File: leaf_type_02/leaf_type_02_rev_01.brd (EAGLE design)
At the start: 35.4 x 21.2 mm, 25 parts, among them J1 TC_2050_IDC_NL_TOP, J3 CONN_4X1_JST_PA, J4 CONN_4X1_JST_PA, J5 CONN_4X1_LEAF_SMT, U2 RS485_XCVR_SN65HVD178X

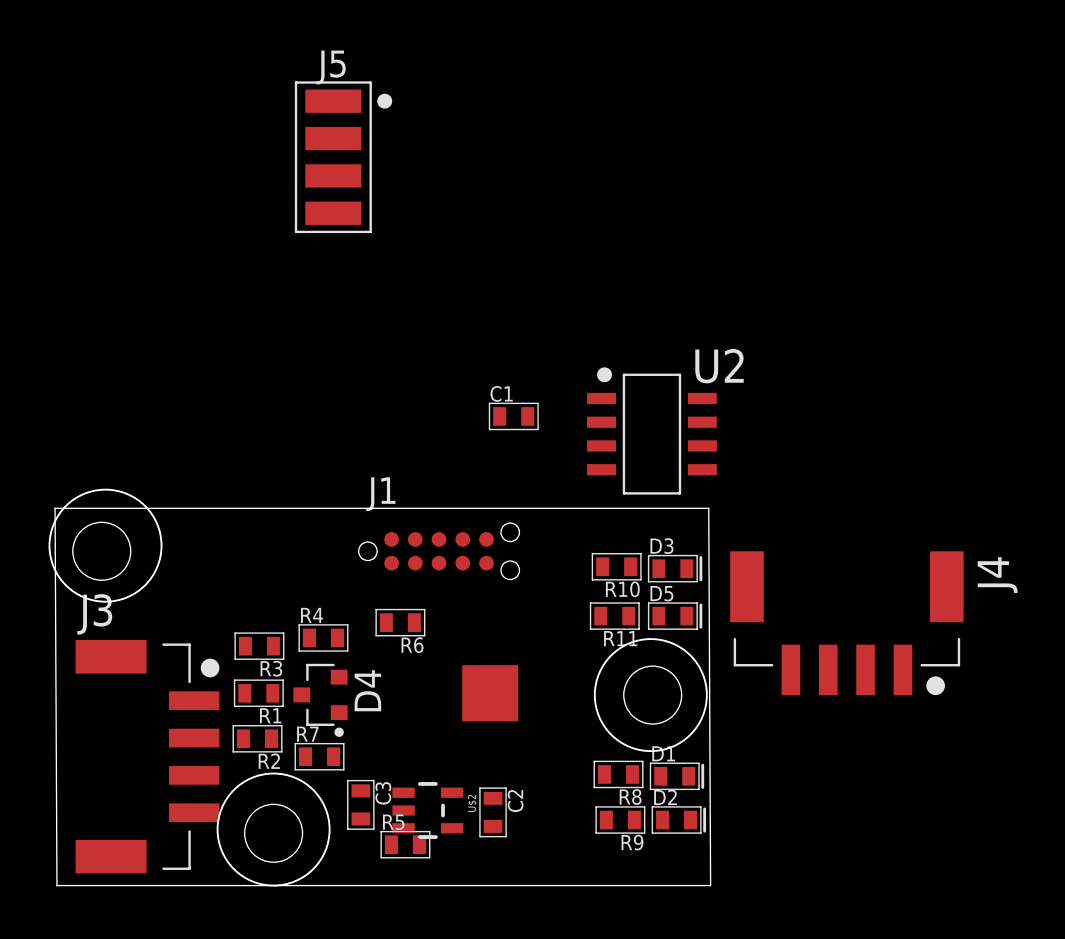
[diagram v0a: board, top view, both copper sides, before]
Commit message: updated library & type 02
fixed some of the sizes of device names, updates rs485 tx & rx drivers
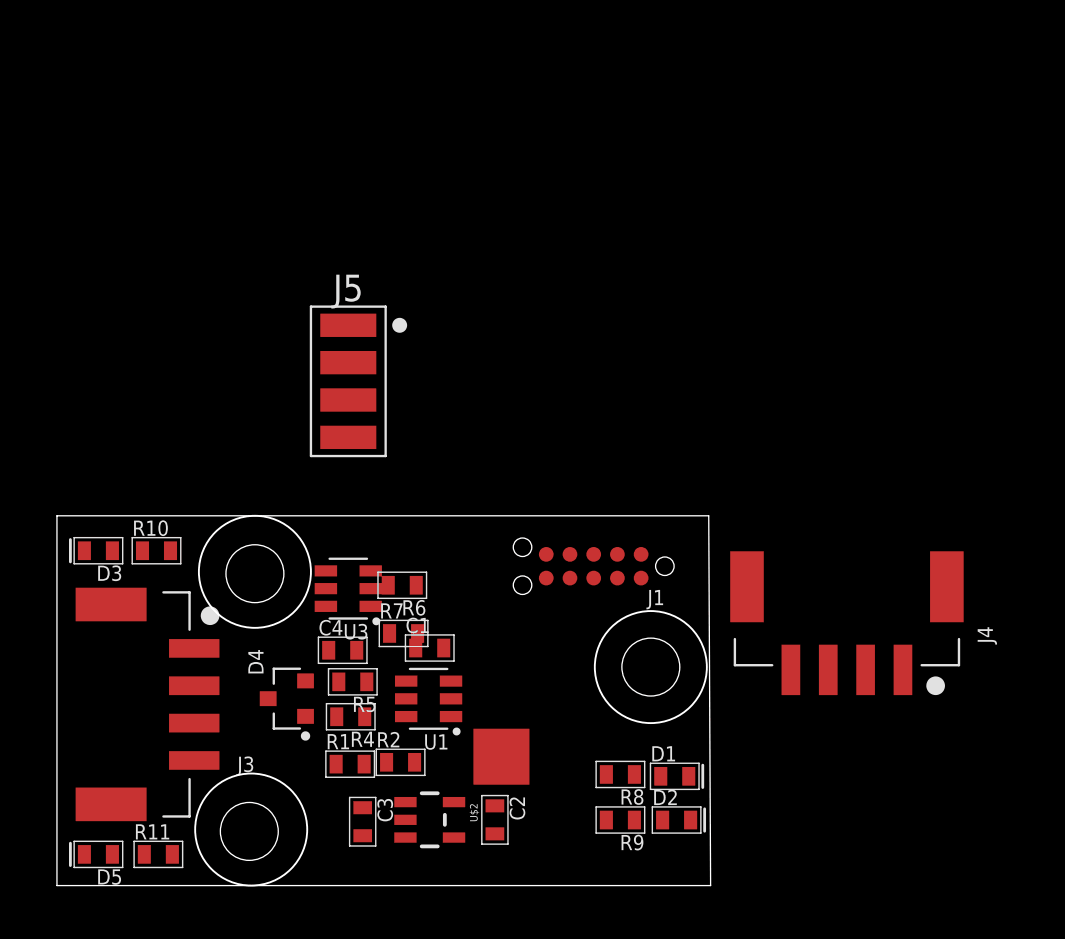
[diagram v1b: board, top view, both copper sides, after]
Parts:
- removed R3: (no value), stepOSP:0603
- removed U2: RS485_XCVR_SN65HVD178X, leaf:SOIC_08_TI
- added C4: 0.1u, stepOSP:0603
- added U1: RS485_RCVR_ISL32612E, leaf:SOT23-6_INTERSIL
- added U3: RS485_TCVR_ISL32614E, leaf:SOT23-6_INTERSIL
- R1: value 120 -> 3.3k
- R2: value (none) -> NP
- R6: value 3.3k -> NP
- moved D5 33.3 mm to (2.22, 1.67), turned to 180 degrees
- moved D3 30.8 mm to (2.22, 17.9), turned to 180 degrees
- moved R11 27.6 mm to (5.43, 1.67), turned to 0 degrees
- moved R10 24.7 mm to (5.33, 17.9), turned to 0 degrees
- moved J1 15.9 mm to (32.5, 17.1), turned to 180 degrees
- moved C1 13.2 mm to (20.0, 12.7)
- moved J5 12.0 mm to (15.6, 27.0)
- moved R5 9.16 mm to (15.8, 10.9), turned to 180 degrees
- moved R7 7.99 mm to (18.6, 13.5)
- moved R2 7.76 mm to (18.4, 6.60), turned to 0 degrees
- moved R1 6.19 mm to (15.7, 6.50), turned to 0 degrees
- moved R4 4.47 mm to (15.7, 9.04), turned to 180 degrees
- moved J3 2.80 mm to (-1.80, 9.70)
- moved R6 2.00 mm to (18.5, 16.1)
- moved D4 1.81 mm to (12.3, 10.0)
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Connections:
- removed net N$10: U2.4
- removed net N$6: D4.2, R1.P$1, R3.P$2, R4.P$2
- removed net N$9: R6.P$1, U2.1
- new net RX: R2.P$1, U1.3
- new net RXE: R1.P$2, R6.P$1, U1.5
- new net TX: U3.1
- new net TXE: R7.P$2, U3.3
- net +3V3: now also C4.P$1, U1.1, U3.2; no longer U2.8
- net GND1: now also C4.P$2, J5.1, R1.P$1, U1.2, U3.5; no longer R3.P$1, U2.5
- net N$1: now also U1.6, U3.6; no longer U2.6
- net N$2: now also U1.4, U3.4; no longer U2.7
- net N$7: now also D4.2, J5.3; no longer D4.1, R1.P$2, R2.P$1
- net N$8: now also D4.1, J5.2, R4.P$2; no longer R7.P$2, U2.2, U2.3
- net V+: now also J5.4
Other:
- board size 35.4 x 21.2 mm -> 35 x 19.8 mm

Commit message: added to library GH connector and updated 0x02 board layout
gh connector only can handle 1A which isn't great but very small
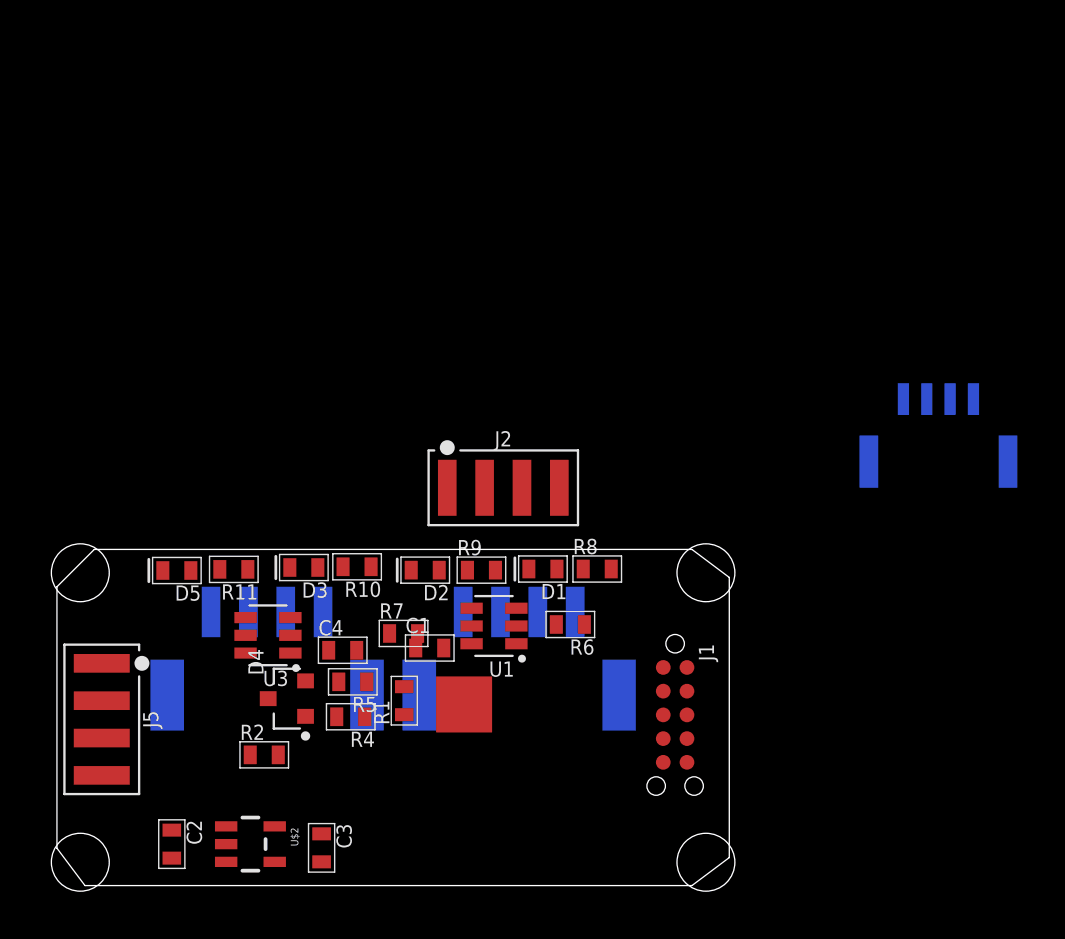
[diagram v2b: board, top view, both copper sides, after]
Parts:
- added J2: CONN_4X1_LEAF_SMT, leaf:CONN_4X1_LEAF_SMT
- added J6: CONN_4X1_JST_GH, leaf:CONN_4X1_JST_GH
- moved J4 34.6 mm to (11.2, 5.50), flipped to the bottom, turned to 180 degrees
- moved J3 26.9 mm to (24.8, 5.50), flipped to the bottom, turned to 180 degrees
- moved J5 22.4 mm to (2.40, 8.90)
- moved D2 19.0 mm to (19.7, 16.9), turned to 180 degrees
- moved C2 17.3 mm to (6.15, 2.22)
- moved R11 15.8 mm to (9.47, 16.9), turned to 180 degrees
- moved D5 15.8 mm to (6.42, 16.9)
- moved R9 15.3 mm to (22.7, 16.9), turned to 0 degrees
- moved D1 13.2 mm to (26.0, 16.9), turned to 180 degrees
- moved R8 11.1 mm to (28.9, 16.9), turned to 0 degrees
- moved D3 11.0 mm to (13.2, 17.0)
- moved R10 10.8 mm to (16.1, 17.1), turned to 180 degrees
- moved U$2 9.69 mm to (10.4, 2.22)
- moved R6 9.24 mm to (27.5, 14.0)
- moved R2 7.31 mm to (11.1, 7.00)
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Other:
- board size 35 x 19.8 mm -> 36 x 18 mm

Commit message: WORK IN PROGRESS
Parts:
- removed C1: 0.1u, stepOSP:0603
- removed J1: TC_2050_IDC_NL_TOP, leaf:TC_2050_IDC_NL_TOP
- removed J4: CONN_4X1_JST_PA, leaf:CONN_4X1_JST_PA
- removed J5: CONN_4X1_LEAF_SMT, leaf:CONN_4X1_LEAF_SMT
- removed R2, R6: NP, stepOSP:0603
- removed U3: RS485_TCVR_ISL32614E, leaf:SOT23-6_INTERSIL
- J2: value CONN_4X1_LEAF_SMT -> TC_2030_IDC_NL_TOP; device leaf:CONN_4X1_LEAF_SMT -> leaf:TC_2030_IDC_NL_TOP
- J3: value CONN_4X1_JST_PA -> CONN_4X1_JST_GH; device leaf:CONN_4X1_JST_PA -> leaf:CONN_4X1_JST_GH
- U1: value RS485_RCVR_ISL32612E -> RS485_XCVR_SN65HVD178X; device leaf:SOT23-6_INTERSIL -> leaf:SOIC_08_TI
- moved J6 32.0 mm to (19.2, 5.90)
- moved U1 18.8 mm to (5.80, 7.40), turned to 0 degrees
- moved J2 16.4 mm to (27.8, 5.40), turned to 90 degrees
- moved J3 15.6 mm to (9.20, 5.90)
- moved D5 15.0 mm to (21.1, 13.7), turned to 270 degrees
- moved R5 14.4 mm to (2.04, 6.71)
- moved C3 14.2 mm to (5.43, 13.2), turned to 90 degrees
- moved R1 14.1 mm to (6.80, 2.10), turned to 0 degrees
- moved R4 13.9 mm to (1.87, 10.6)
- moved R11 13.3 mm to (21.2, 10.6), turned to 90 degrees
- moved C2 11.7 mm to (8.45, 13.7)
- moved U$2 11.5 mm to (12.7, 13.5)
- moved D4 10.8 mm to (1.89, 6.99), flipped to the bottom, turned to 270 degrees
- moved R7 10.8 mm to (11.5, 5.36), turned to 90 degrees
- moved D3 10.2 mm to (22.9, 13.7), turned to 270 degrees
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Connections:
- removed net N$11: D5.P$1, R11.P$1
- removed net N$8: D4.1, J5.2, R4.P$2
- removed net RX: R2.P$1, U1.3
- removed net RXE: R1.P$2, R6.P$1, U1.5
- removed net TX: U3.1
- removed net TXE: R7.P$2, U3.3
- new net N$10: R7.P$2, U1.2, U1.3
- new net N$12: R1.P$1, U1.1
- new net N$13: U1.4
- new net N$6: R4.P$1, U1.7
- new net N$9: R5.P$1, U1.6
- net +3V3: now also D1.P$1, D2.P$1, D3.P$1, D5.P$1, R1.P$2, U1.8; no longer C1.P$1, R2.P$2, R6.P$2, U1.1, U3.2
- net GND1: now also J3.1, J6.1, U1.5; no longer C1.P$2, J5.1, R1.P$1, U1.2, U3.5
- net N$1: now also D4.1, J3.3, J6.3, R4.P$2; no longer R4.P$1, U1.6, U3.6
- net N$2: now also D1.P$2, R8.P$2; no longer R5.P$1, U1.4, U3.4
- net N$3: now also D2.P$2, R9.P$2; no longer D1.P$1, R8.P$1
- net N$4: now also D3.P$2, R10.P$2; no longer D2.P$1, R9.P$1
- net N$5: now also D5.P$2, R11.P$2; no longer D3.P$1, R10.P$1
- net N$7: now also J3.2, J6.2; no longer J5.3
- net V+: now also J3.4; no longer J5.4
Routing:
- net N$1: track 0.00 -> 36.2 mm, vias 0 -> 3
- net N$7: track 0.00 -> 26.9 mm, vias 0 -> 1
- net +3V3: track 0.00 -> 26.5 mm
- net N$9: track 0.00 -> 8.94 mm
- net N$6: track 0.00 -> 8.77 mm
- net V+: track 0.00 -> 8.68 mm, vias 0 -> 1
- net N$10: track 0.00 -> 7.25 mm
- net N$12: track 0.00 -> 2.70 mm
- net N$2: track 0.00 -> 1.73 mm
- net N$4: track 0.00 -> 1.69 mm
- net N$5: track 0.00 -> 1.63 mm
- net N$3: track 0.00 -> 1.59 mm
- added copper zone on layer 1, net GND1
- added copper zone on layer 16, net GND1
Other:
- board size 36 x 18 mm -> 30 x 16 mm

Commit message: updating 0x02 build
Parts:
- removed D3, D5: 0603_LED, stepOSP:0603_LED
- removed J3, J6: CONN_4X1_JST_GH, leaf:CONN_4X1_JST_GH
- removed R10, R11: (no value), stepOSP:0603
- added J1: TC_2050_IDC_NL_TOP, leaf:TC_2050_IDC_NL_TOP
- added J4, J5: CONN_4X1_JST_PA, leaf:CONN_4X1_JST_PA
- J2: value TC_2030_IDC_NL_TOP -> CONN_5X2_0P05_IN_SMT; device leaf:TC_2030_IDC_NL_TOP -> leaf:CONN_5X2_0P050_IN_SMT
- R1, R7, R8, R9: device stepOSP:0603 -> stepOSP:0402
- moved J2 17.3 mm to (12.8, 14.0), turned to 270 degrees
- moved R9 13.7 mm to (5.57, 10.2), turned to 180 degrees
- moved D1 11.3 mm to (18.7, 4.05), turned to 180 degrees
- moved C3 10.7 mm to (4.37, 2.52), turned to 270 degrees
- moved C2 10.7 mm to (18.9, 11.4), flipped to the bottom, turned to 180 degrees
- moved R8 10.5 mm to (17.4, 2.95), turned to 180 degrees
- moved C4 8.79 mm to (19.2, 5.30), flipped to the bottom, turned to 180 degrees
- moved R1 8.74 mm to (15.5, 2.90)
- moved U$2 8.10 mm to (19.0, 8.46), flipped to the bottom, turned to 180 degrees
- moved R7 3.92 mm to (15.4, 4.96)
- moved R4 2.41 mm to (2.54, 12.9), flipped to the bottom, turned to 90 degrees
- moved D4 2.33 mm to (2.89, 9.09)
- moved D2 2.19 mm to (18.0, 15.5), turned to 180 degrees
- moved R5 1.16 mm to (2.71, 5.76), flipped to the bottom, turned to 270 degrees
- moved U1 0.32 mm to (5.90, 7.70), turned to 90 degrees
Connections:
- removed net N$4: D3.P$2, R10.P$2
- removed net N$5: D5.P$2, R11.P$2
- net +3V3: no longer D3.P$1, D5.P$1
- net GND1: now also J4.2, J5.3; no longer J3.1, J6.1
- net N$1: now also J4.4, J5.1; no longer J3.3, J6.3
- net N$7: now also J4.3, J5.2; no longer J3.2, J6.2
- net V+: now also J4.1, J5.4; no longer J3.4
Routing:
- net N$1: track 36.2 -> 3.80 mm, vias 3 -> 0
- net +3V3: track 26.5 -> 0.00 mm
- net N$7: track 26.9 -> 3.80 mm, vias 1 -> 0
- net N$9: track 8.94 -> 0.00 mm
- net N$6: track 8.77 -> 0.00 mm
- net N$10: track 7.25 -> 0.00 mm
- net V+: track 8.68 -> 5.91 mm, vias 1 -> 0
- net N$12: track 2.70 -> 0.00 mm
- net N$2: track 1.73 -> 0.00 mm
- net N$4: track 1.69 -> 0.00 mm
- net N$5: track 1.63 -> 0.00 mm
- net N$3: track 1.59 -> 0.00 mm
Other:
- board size 30 x 16 mm -> 26.5 x 18.5 mm

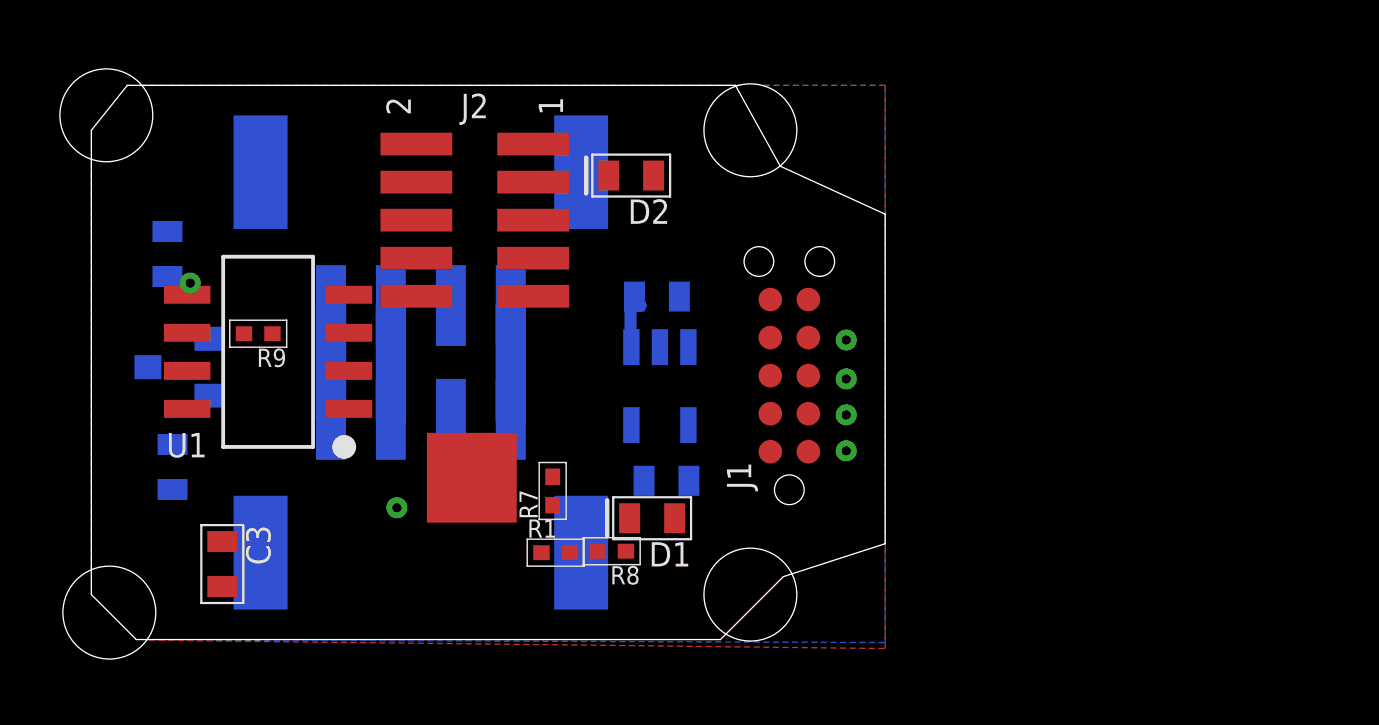
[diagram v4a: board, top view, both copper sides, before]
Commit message: stm32 part update
added stm32l031G6U6 part and added footprints for qfn 28, 32 & tfqp 32
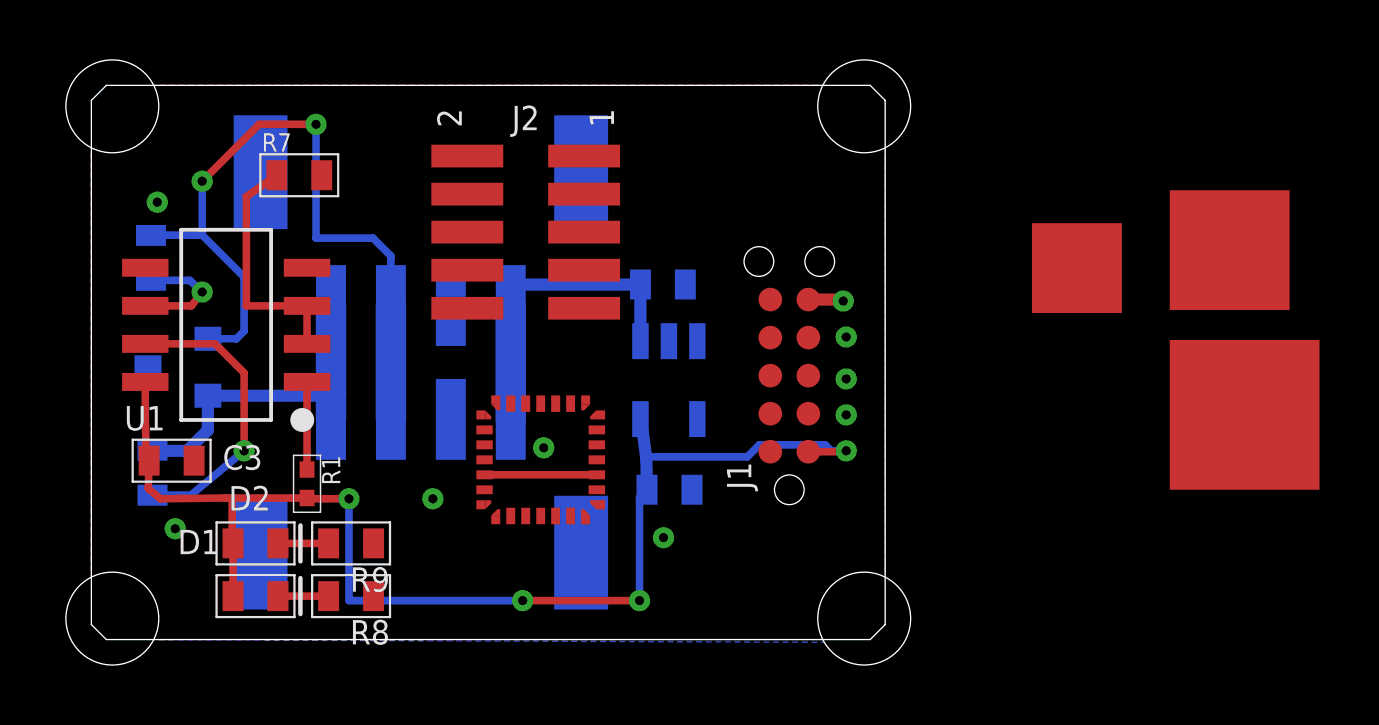
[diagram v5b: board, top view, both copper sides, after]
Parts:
- added U2: STM32L031G6U6, leaf:STM32_QFN_28_4X4
- R7, R8, R9: device stepOSP:0402 -> stepOSP:0603
- moved D2 17.6 mm to (5.48, 3.21), turned to 0 degrees
- moved R7 13.5 mm to (6.94, 15.5), turned to 180 degrees
- moved D1 13.5 mm to (5.48, 1.45), turned to 0 degrees
- moved R8 8.83 mm to (8.67, 1.45)
- moved R1 8.61 mm to (7.20, 5.20), turned to 270 degrees
- moved R9 7.66 mm to (8.67, 3.21)
- moved R4 7.32 mm to (2.04, 5.57)
- moved R5 7.02 mm to (1.99, 12.7), turned to 90 degrees
- moved C3 3.84 mm to (2.68, 5.97), turned to 0 degrees
- moved J2 1.75 mm to (14.5, 13.6)
- moved U1 1.66 mm to (4.50, 8.60)
- moved C2 0.45 mm to (19.1, 11.8)
- moved U$2 0.36 mm to (19.3, 8.66)
- moved C4 0.32 mm to (19.3, 5.00)
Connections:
- new net DBG_RX: J1.9
- new net DBG_TX: J1.8
- new net HRT_B: J1.7
- new net N_RESET: J1.10
- new net SWO: J1.6
- new net SW_CLK: J1.4, U2.22
- new net SW_DIO: J1.2, U2.21
- net +3V3: now also J1.1, J2.4, U2.17, U2.5
- net GND1: now also J1.3, J1.5, J2.1, U2.16
- net N$1: now also D4.2; no longer D4.1
- net N$7: now also D4.1; no longer D4.2
- net V+: now also J2.2
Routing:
- net +3V3: track 0.00 -> 45.6 mm, vias 0 -> 4
- net N$7: track 3.80 -> 25.2 mm, vias 0 -> 2
- net N$6: track 0.00 -> 9.90 mm, vias 0 -> 1
- net N$10: track 0.00 -> 8.18 mm
- net N$1: track 3.80 -> 11.2 mm
- net V+: track 5.91 -> 10.7 mm
- net N$9: track 0.00 -> 3.99 mm, vias 0 -> 1
- net N$12: track 0.00 -> 2.92 mm
- net N$3: track 0.00 -> 1.69 mm
- net N$2: track 0.00 -> 1.69 mm
- net GND1: track 0.00 -> 1.22 mm, vias 6 -> 7
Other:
- outline, holes or cut-outs redrawn
